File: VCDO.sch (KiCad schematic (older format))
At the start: 68 parts, among them J1 PCB INTERCONNECT, J2 PROGRAMMING HEADER, Q1 2N3904, U1 TL074, U2 Druid VCDO, U3 TL074, U4 TL072

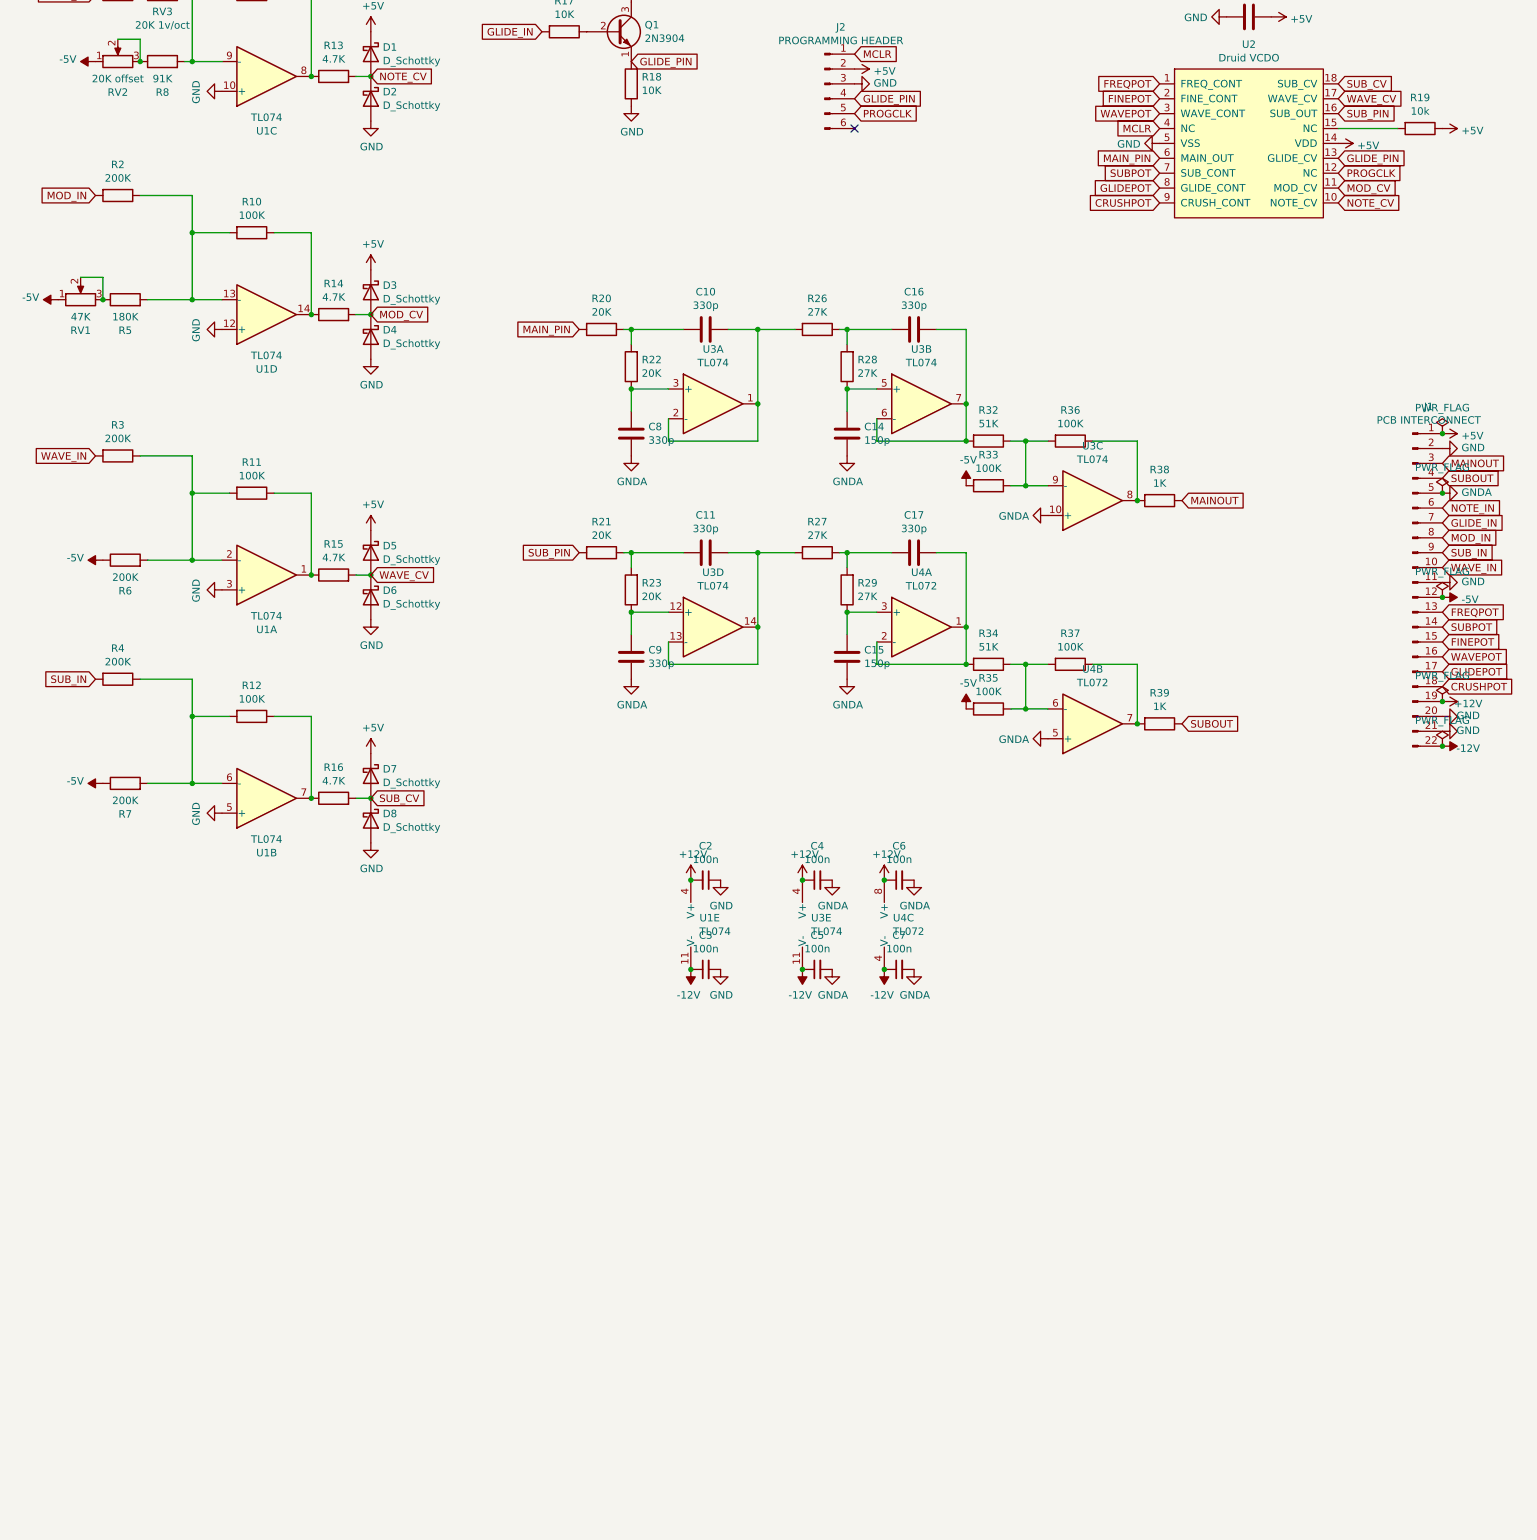
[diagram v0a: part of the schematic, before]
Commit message: remove daughter conn, add att pots
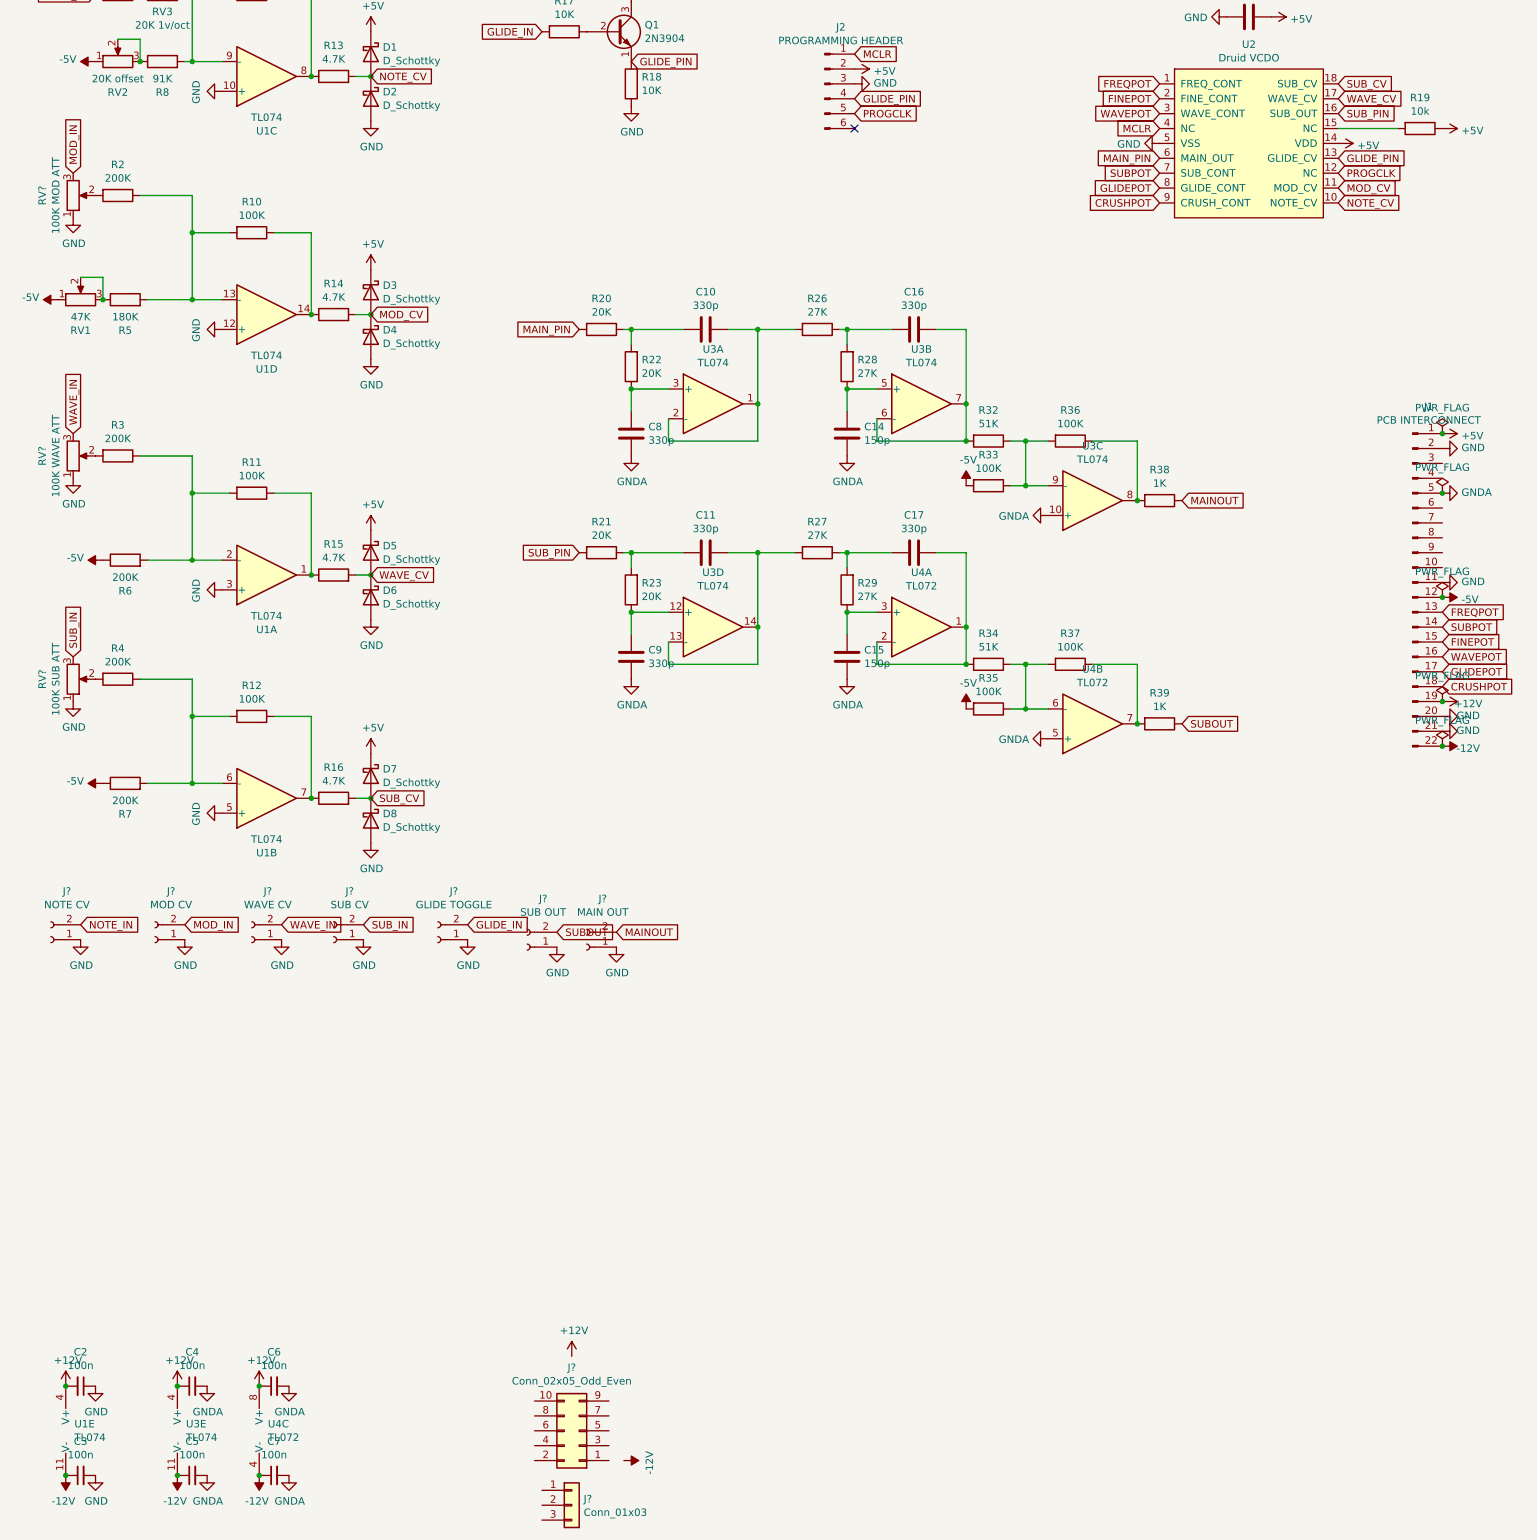
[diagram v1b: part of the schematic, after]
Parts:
- added J?: NOTE CV, symbol Connector:Conn_01x02_Female
- added J?: MOD CV, symbol Connector:Conn_01x02_Female
- added J?: WAVE CV, symbol Connector:Conn_01x02_Female
- added J?: SUB CV, symbol Connector:Conn_01x02_Female
- added J?: SUB OUT, symbol Connector:Conn_01x02_Female
- added J?: MAIN OUT, symbol Connector:Conn_01x02_Female
- added J?: GLIDE TOGGLE, symbol Connector:Conn_01x02_Female
- added J?: Conn_02x05_Odd_Even, symbol Connector_Generic:Conn_02x05_Odd_Even
- added J?: Conn_01x03, symbol Connector_Generic:Conn_01x03
- added RV?: 100K MOD ATT, Potentiometer_THT:Potentiometer_Bourns_3296W_Vertical, symbol Device:R_POT
- added RV?: 100K WAVE ATT, Potentiometer_THT:Potentiometer_Bourns_3296W_Vertical, symbol Device:R_POT
- added RV?: 100K SUB ATT, Potentiometer_THT:Potentiometer_Bourns_3296W_Vertical, symbol Device:R_POT
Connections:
- net GLIDE_IN: now also J?.2 (Pin_2); no longer J1.7 (Pin_7)
- net GND: now also J?.1 (Pin_1), J?.1 (Pin_1), J?.1 (Pin_1), J?.1 (Pin_1), J?.1 (Pin_1), J?.1 (Pin_1), J?.1 (Pin_1), RV?.1, RV?.1, RV?.1
- net MAINOUT: now also J?.2 (Pin_2); no longer J1.3 (Pin_3)
- net MOD_IN: now also J?.2 (Pin_2), RV?.3; no longer J1.8 (Pin_8), R2.2
- net NOTE_IN: now also J?.2 (Pin_2); no longer J1.6 (Pin_6)
- net SUBOUT: now also J?.2 (Pin_2); no longer J1.4 (Pin_4)
- net SUB_IN: now also J?.2 (Pin_2), RV?.3; no longer J1.9 (Pin_9), R4.2
- net WAVE_IN: now also J?.2 (Pin_2), RV?.3; no longer J1.10 (Pin_10), R3.2
- new net: R2.2, RV?.2
- new net: R3.2, RV?.2
- new net: R4.2, RV?.2
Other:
- moved on the sheet: C2, C3, C4, C5, C6, C7, U1E, U3E, U4C

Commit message: power
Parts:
- J?: value Conn_02x05_Odd_Even -> SYNTH POWER
- J?: value Conn_01x03 -> TEST HEADER
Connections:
- net +12V: now also J?.1 (Pin_1), J?.10 (Pin_10), J?.9 (Pin_9)
- net -12V: now also J?.1 (Pin_1), J?.2 (Pin_2), J?.3 (Pin_3)
- net GND: now also J?.2 (Pin_2), J?.3 (Pin_3), J?.4 (Pin_4), J?.5 (Pin_5), J?.6 (Pin_6), J?.7 (Pin_7), J?.8 (Pin_8)
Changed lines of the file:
@@
 P 4300 10500
 F 0 "J?" H 4350 10075 50  0000 C CNN
-F 1 "Conn_02x05_Odd_Even" H 4350 10166 50  0000 C CNN
+F 1 "SYNTH POWER" H 4350 10166 50  0000 C CNN
 F 2 "" H 4300 10500 50  0001 C CNN
 F 3 "~" H 4300 10500 50  0001 C CNN
@@
 P 4250 11000
 F 0 "J?" H 4330 11042 50  0000 L CNN
-F 1 "Conn_01x03" H 4330 10951 50  0000 L CNN
+F 1 "TEST HEADER" H 4330 10951 50  0000 L CNN
 F 2 "" H 4250 11000 50  0001 C CNN
 F 3 "~" H 4250 11000 50  0001 C CNN
@@
 	1    0    0    -1
 $EndComp
+$Comp
+L power:GND #PWR?
+U 1 1 60C1CF07
+P 4600 10500
+F 0 "#PWR?" H 4600 10250 50  0001 C CNN
+F 1 "GND" H 4605 10327 50  0000 C CNN
+F 2 "" H 4600 10500 50  0001 C CNN
+F 3 "" H 4600 10500 50  0001 C CNN
+	1    4600 10500
+	0    -1   -1   0
+$EndComp
+Wire Wire Line
+	4500 10600 4600 10600
+Wire Wire Line
+	4600 10600 4600 10500
+Wire Wire Line
+	4500 10500 4600 10500
+Connection ~ 4600 10500
+Wire Wire Line
+	4600 10400 4600 10500
+Wire Wire Line
+	4000 10400 4500 10400
+Connection ~ 4500 10400
+Wire Wire Line
+	4500 10400 4600 10400
+Wire Wire Line
+	4000 10500 4500 10500
+Connection ~ 4500 10500
+Wire Wire Line
+	4000 10600 4500 10600
+Connection ~ 4500 10600
+Wire Wire Line
+	4000 10700 4000 10800
+Wire Wire Line
+	4000 10800 4500 10800
+Wire Wire Line
+	4500 10800 4500 10700
+Wire Wire Line
+	4600 10700 4500 10700
+Connection ~ 4500 10700
+Wire Wire Line
+	4000 10300 4000 10000
+Wire Wire Line
+	4000 10000 4250 10000
+Wire Wire Line
+	4250 10000 4500 10000
+Wire Wire Line
+	4500 10000 4500 10300
+Connection ~ 4250 10000
+$Comp
+L power:+12V #PWR?
+U 1 1 60C4A7CC
+P 4050 10900
+F 0 "#PWR?" H 4050 10750 50  0001 C CNN
+F 1 "+12V" H 4065 11073 50  0000 C CNN
+F 2 "" H 4050 10900 50  0001 C CNN
+F 3 "" H 4050 10900 50  0001 C CNN
+	1    4050 10900
+	0    -1   -1   0
+$EndComp
+$Comp
+L power:GND #PWR?
+U 1 1 60C4B078
+P 4050 11000
+F 0 "#PWR?" H 4050 10750 50  0001 C CNN
+F 1 "GND" H 4055 10827 50  0000 C CNN
+F 2 "" H 4050 11000 50  0001 C CNN
+F 3 "" H 4050 11000 50  0001 C CNN
+	1    4050 11000
+	0    1    1    0
+$EndComp
+$Comp
+L power:-12V #PWR?
+U 1 1 60C4B707
+P 4050 11100
+F 0 "#PWR?" H 4050 11200 50  0001 C CNN
+F 1 "-12V" H 4065 11273 50  0000 C CNN
+F 2 "" H 4050 11100 50  0001 C CNN
+F 3 "" H 4050 11100 50  0001 C CNN
+	1    4050 11100
+	0    -1   -1   0
+$EndComp
 $EndSCHEMATC

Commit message: regulators
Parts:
- added C? (x2): 100uF, symbol Device:CP_Small
- added U?: L7905, symbol Regulator_Linear:L7905
- added U?: L7805, symbol Regulator_Linear:L7805
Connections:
- net +12V: now also C?.1, U?.1 (IN)
- net -5V: now also C?.1, U?.3 (OUT)
- net GND: now also C?.2, C?.2, U?.1 (GND), U?.2 (GND)
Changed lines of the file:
@@
 	0    -1   -1   0
 $EndComp
+$Comp
+L Regulator_Linear:L7905 U?
+U 1 1 60C4C789
+P 6950 10550
+F 0 "U?" H 6950 10308 50  0000 C CNN
+F 1 "L7905" H 6950 10399 50  0000 C CNN
+F 2 "" H 6950 10350 50  0001 C CIN
+F 3 "http://www.st.com/content/ccc/resource/technical/document/datasheet/c9/16/86/41/c7/2b/45/f2/CD00000450.pdf/files/CD00000450.pdf/jcr:content/translations/en.CD00000450.pdf" H 6950 10550 50  0001 C CNN
+	1    6950 10550
+	1    0    0    1
+$EndComp
+$Comp
+L Regulator_Linear:L7805 U?
+U 1 1 60C4FB0A
+P 8700 10500
+F 0 "U?" H 8700 10742 50  0000 C CNN
+F 1 "L7805" H 8700 10651 50  0000 C CNN
+F 2 "" H 8725 10350 50  0001 L CIN
+F 3 "http://www.st.com/content/ccc/resource/technical/document/datasheet/41/4f/b3/b0/12/d4/47/88/CD00000444.pdf/files/CD00000444.pdf/jcr:content/translations/en.CD00000444.pdf" H 8700 10450 50  0001 C CNN
+	1    8700 10500
+	1    0    0    -1
+$EndComp
+$Comp
+L power:-12V #PWR?
+U 1 1 60C5630C
+P 6600 10550
+F 0 "#PWR?" H 6600 10650 50  0001 C CNN
+F 1 "-12V" H 6615 10723 50  0000 C CNN
+F 2 "" H 6600 10550 50  0001 C CNN
+F 3 "" H 6600 10550 50  0001 C CNN
+	1    6600 10550
+	1    0    0    -1
+$EndComp
+$Comp
+L power:GND #PWR?
+U 1 1 60C56A22
+P 6950 10850
+F 0 "#PWR?" H 6950 10600 50  0001 C CNN
+F 1 "GND" H 6955 10677 50  0000 C CNN
+F 2 "" H 6950 10850 50  0001 C CNN
+F 3 "" H 6950 10850 50  0001 C CNN
+	1    6950 10850
+	1    0    0    -1
+$EndComp
+$Comp
+L power:+12V #PWR?
+U 1 1 60C56E9F
+P 8400 10500
+F 0 "#PWR?" H 8400 10350 50  0001 C CNN
+F 1 "+12V" H 8415 10673 50  0000 C CNN
+F 2 "" H 8400 10500 50  0001 C CNN
+F 3 "" H 8400 10500 50  0001 C CNN
+	1    8400 10500
+	1    0    0    -1
+$EndComp
+$Comp
+L power:GND #PWR?
+U 1 1 60C57378
+P 8700 10800
+F 0 "#PWR?" H 8700 10550 50  0001 C CNN
+F 1 "GND" H 8705 10627 50  0000 C CNN
+F 2 "" H 8700 10800 50  0001 C CNN
+F 3 "" H 8700 10800 50  0001 C CNN
+	1    8700 10800
+	1    0    0    -1
+$EndComp
+$Comp
+L power:-5V #PWR?
+U 1 1 60C5778D
+P 9300 10500
+F 0 "#PWR?" H 9300 10600 50  0001 C CNN
+F 1 "-5V" V 9315 10628 50  0000 L CNN
+F 2 "" H 9300 10500 50  0001 C CNN
+F 3 "" H 9300 10500 50  0001 C CNN
+	1    9300 10500
+	0    1    1    0
+$EndComp
+$Comp
+L Device:CP_Small C?
+U 1 1 60C581D6
+P 8400 10600
+F 0 "C?" H 8488 10646 50  0000 L CNN
+F 1 "100uF" H 8488 10555 50  0000 L CNN
+F 2 "" H 8400 10600 50  0001 C CNN
+F 3 "~" H 8400 10600 50  0001 C CNN
+	1    8400 10600
+	1    0    0    -1
+$EndComp
+Connection ~ 8400 10500
+Wire Wire Line
+	8400 10700 8400 10800
+Wire Wire Line
+	8400 10800 8700 10800
+Connection ~ 8700 10800
+$Comp
+L Device:CP_Small C?
+U 1 1 60C5EDE3
+P 9000 10600
+F 0 "C?" H 9088 10646 50  0000 L CNN
+F 1 "100uF" H 9088 10555 50  0000 L CNN
+F 2 "" H 9000 10600 50  0001 C CNN
+F 3 "~" H 9000 10600 50  0001 C CNN
+	1    9000 10600
+	1    0    0    -1
+$EndComp
+Connection ~ 9000 10500
+Wire Wire Line
+	8700 10800 9000 10800
+Wire Wire Line
+	9000 10800 9000 10700
+Wire Wire Line
+	9300 10500 9000 10500
 $EndSCHEMATC
